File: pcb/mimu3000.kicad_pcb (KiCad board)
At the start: 2 copper layers, 54.8 x 40 mm, 19 parts, among them J1 OPT, SW1 ONOFF, SW2 SW_DPDT_x2, U1 AQY211EH, U2 ATTINY88AU

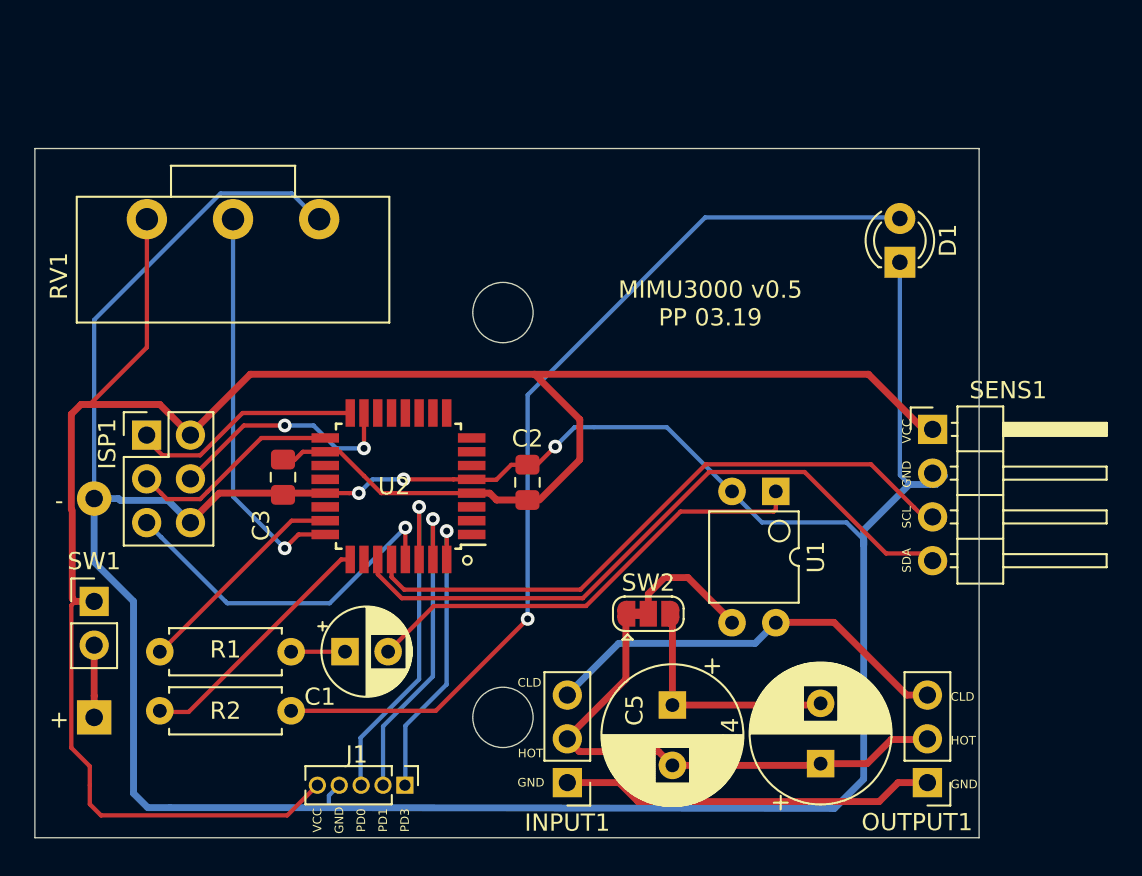
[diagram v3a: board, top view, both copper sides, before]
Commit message: Fixed misconception that a Capacitor before Opto would smooth the curve
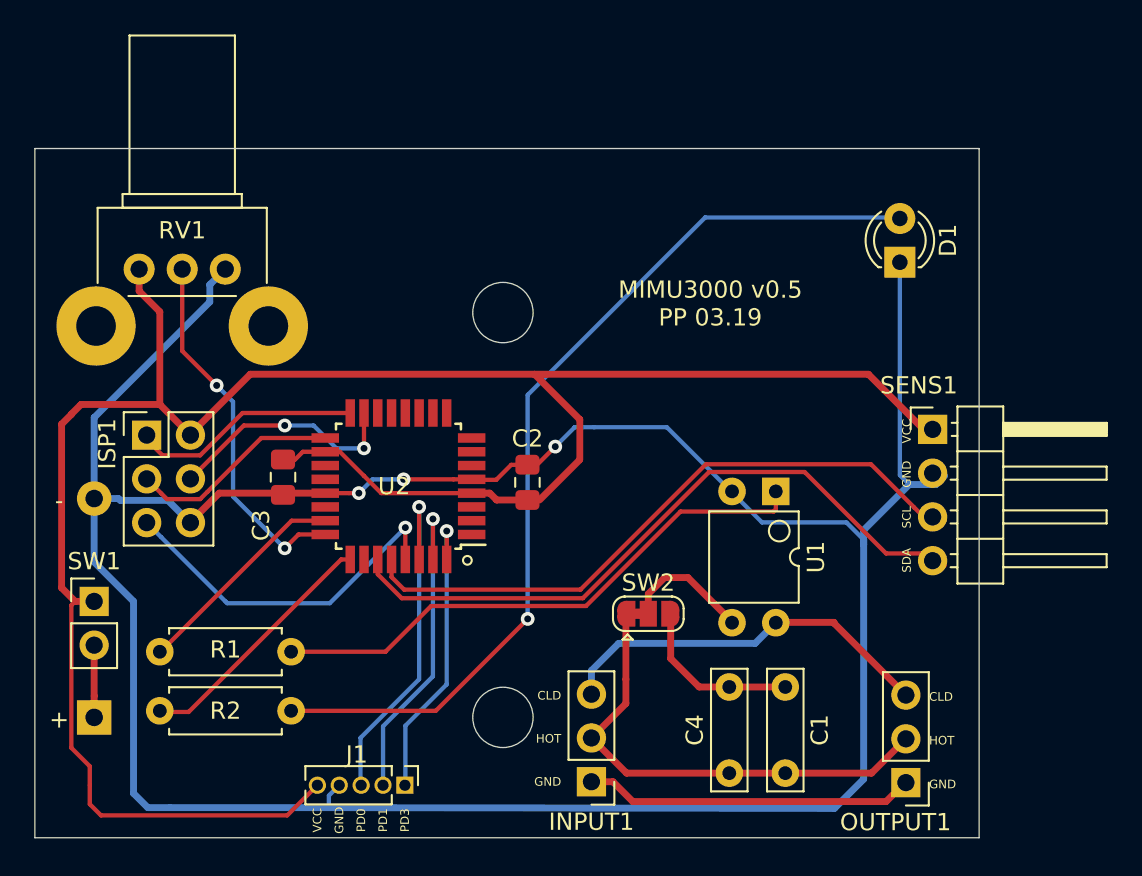
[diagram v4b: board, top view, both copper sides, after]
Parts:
- removed C5: 1000uF, Capacitor_THT:CP_Radial_D8.0mm_P3.50mm
- C1: value 47µ -> 1uF; footprint Capacitor_THT:CP_Radial_D5.0mm_P2.50mm -> Capacitors_THT:C_Rect_L7.0mm_W2.0mm_P5.00mm
- C4: value 1000uF -> 1uF; footprint Capacitor_THT:CP_Radial_D8.0mm_P3.50mm -> Capacitors_THT:C_Rect_L7.0mm_W2.0mm_P5.00mm
- RV1: footprint custom:Potentiometer_Generic_5mm_Single_Horizontal -> Potentiometers:Potentiometer_Bourns_PTV09A-2_Vertical
- moved C1 26.5 mm to (207.8, 123.2), turned to 90 degrees
- moved RV1 6.17 mm to (175.2, 94.0)
- moved C4 5.33 mm to (204.5, 123.2)
- moved INPUT1 1.40 mm to (196.5, 123.8)
- moved OUTPUT1 1.25 mm to (214.8, 123.8)
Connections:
- C4 pad 1: Net-(C4-Pad1) -> Net-(C1-Pad1)
- C4 pad 2: Net-(C4-Pad2) -> Net-(C1-Pad2)
- INPUT1 pad 2: Net-(C4-Pad1) -> Net-(C1-Pad1)
- OUTPUT1 pad 2: Net-(C4-Pad1) -> Net-(C1-Pad1)
- R1 pad 2: Net-(C1-Pad1) -> Net-(R1-Pad2)
- SW2 pad 1: Net-(C4-Pad1) -> Net-(C1-Pad1)
- SW2 pad 3: Net-(C4-Pad2) -> Net-(C1-Pad2)
- U1 pad 1: Net-(C1-Pad2) -> Net-(R1-Pad2)
- U2 pad 1: (no net) -> Net-(U2-Pad1)
- U2 pad 10: (no net) -> Net-(U2-Pad10)
- U2 pad 11: (no net) -> Net-(U2-Pad11)
- U2 pad 12: (no net) -> Net-(U2-Pad12)
- U2 pad 13: (no net) -> Net-(U2-Pad13)
- U2 pad 14: (no net) -> Net-(U2-Pad14)
- U2 pad 19: (no net) -> Net-(U2-Pad19)
- U2 pad 2: (no net) -> Net-(U2-Pad2)
- U2 pad 20: (no net) -> Net-(U2-Pad20)
- U2 pad 22: (no net) -> Net-(U2-Pad22)
- U2 pad 26: (no net) -> Net-(U2-Pad26)
- U2 pad 3: (no net) -> Net-(U2-Pad3)
- U2 pad 6: (no net) -> Net-(U2-Pad6)
- U2 pad 7: (no net) -> Net-(U2-Pad7)
- U2 pad 8: (no net) -> Net-(U2-Pad8)
- U2 pad 9: (no net) -> Net-(U2-Pad9)
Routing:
- net Net-(R1-Pad2): track 0.00 -> 32.6 mm
- net Net-(C4-Pad1): track 30.5 -> 0.00 mm
- net Net-(C1-Pad1): track 3.12 -> 28.0 mm
- net Net-(C1-Pad2): track 27.0 -> 10.1 mm
- net Net-(C4-Pad2): track 13.7 -> 0.00 mm
- net GND: track 175.0 -> 164.4 mm
- net +3V0: track 130.7 -> 127.4 mm
- net Net-(INPUT1-Pad1): track 21.8 -> 19.2 mm
- net Net-(INPUT1-Pad3): track 24.4 -> 22.5 mm
- net POT: track 23.0 -> 21.3 mm, vias 1 -> 2
